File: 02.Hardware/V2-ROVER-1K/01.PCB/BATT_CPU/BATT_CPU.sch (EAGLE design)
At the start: 70 parts, among them K2 FLEX6, Q1 BSS84W-7-F, Q2 BSS84W-7-F, Q3 2N7002PW, Q4 2N7002PW, Q5 2N7002PW, U1 ATSAMD21G18_QFN, U3 TPS78230DDCR, U6 MAX9062EUK+T, U8 SN74LVC1G19DBVR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

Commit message: Update CPU
Colocacion de transistor a la salida del comparador.
"Multiplexado" de la señal del OP_SWITCH
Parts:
- removed R49: 10K, SparkFun-Resistors:RESISTOR0402
- Q5: value 2N7002PW -> BSS84W-7-F; device SparkFun-DiscreteSemi:MOSFET-NCHANNEL2N7002PW -> BSS84W-7-F:BSS84W-7-F
- R18: value (none) -> 100k
- R48: value 100R -> 10k
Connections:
- removed net A0: U1.PA02/EINT2/AIN0/Y0/VOUT
- removed net CPU_EN_DCDC: R18.2, U1.PA16/I2C/I0/SERCOM1+3.0
- removed net IN_UVLO: Q5.G, R48.2, R49.2, U1.PA21/I5/SERCOM3+5.3/I2SFS0
- removed net N$58: R48.1, U6.OUT
- new net CPU_OP_SWITCH: Q5.G, R18.2, U1.PA17/I2C/I1/SERCOM1+3.1
- new net FB_DAC: K2.P$1, U1.PA02/EINT2/AIN0/Y0/VOUT
- new net N$15: U1.PA21/I5/SERCOM3+5.3/I2SFS0
- new net N$16: Q5.D, R18.1, R48.1, U6.OUT
- net EN_DCDC: now also U1.PA16/I2C/I0/SERCOM1+3.0; no longer Q5.D, R18.1
- net GND: no longer Q5.S, R49.1
- net OP_SWITCH: now also Q5.S; no longer U1.PA17/I2C/I1/SERCOM1+3.1
- net VCC: now also R48.2; no longer K2.P$1
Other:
- moved on the sheet: R18, R48

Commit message: revision inicial
corregido rutado del display
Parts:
- R4: value (none) -> 100k
- R5: value (none) -> 47k
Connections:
- net !RES renamed !RES_OLED
- net CPU_OP_SWITCH renamed !CPU_OP_SWITCH
- removed net VDD: C10.1, C22.1, R6.2, U$30.VDD
- net VBAT_LCD: now also Q2.D; no longer Q2.S
- net VBUS: now also Q2.S; no longer Q2.D
- net VCC_2: now also C10.1, C22.1, R6.2, U$30.VDD
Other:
- moved on the sheet: C10, C22, C24, Q2, R6, VBUS, VBUS1, VBUS2, VBUS3, VBUS4

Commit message: Errors Fix
Polaridad PNP.
Señal Rx cambio por TX.
VDD cambio por VCC_2 Display.
ERC y DRC Check
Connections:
- removed net N$11: U1.PA25/I13/SERCOM3+5.3/D+
- removed net N$12: U1.PA28/I8
- removed net N$13: U1.PB03/I3/AIN11/SERCOM5.1
- removed net N$14: U1.PA24/I12/SERCOM3+5.2/D-
- removed net N$15: U1.PA21/I5/SERCOM3+5.3/I2SFS0
- removed net N$8: U1.PA27/I15
- removed net N$9: U1.PA13/I13/I2C/SERCOM2+4.1
- removed net TST_MODE: U1.PA07/I7/AIN7/SERCOM0.3/I2SD0
- removed net VSS: U$30.VSS
- net !RESET: now also VBUS1.TP
- net GND: now also U$30.VSS, VBUS4.TP
- net N$16: now also Q5.S; no longer Q5.D
- net OP_SWITCH: now also Q5.D; no longer Q5.S
- net RXI: no longer K2.P$7
- net SWCLK: now also VBUS2.TP
- net SWDIO: now also VBUS3.TP
- net S_POWER: now also U1.PA21/I5/SERCOM3+5.3/I2SFS0
- net TXO: now also K2.P$7
- net VCC: now also Q1.S, VBUS.TP; no longer Q1.D
- net VCC_2: now also Q1.D; no longer Q1.S
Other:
- note removed: "N/C"
- note removed: "TXLED"
- note removed: "USBHOSTEN"
- moved on the sheet: Q1

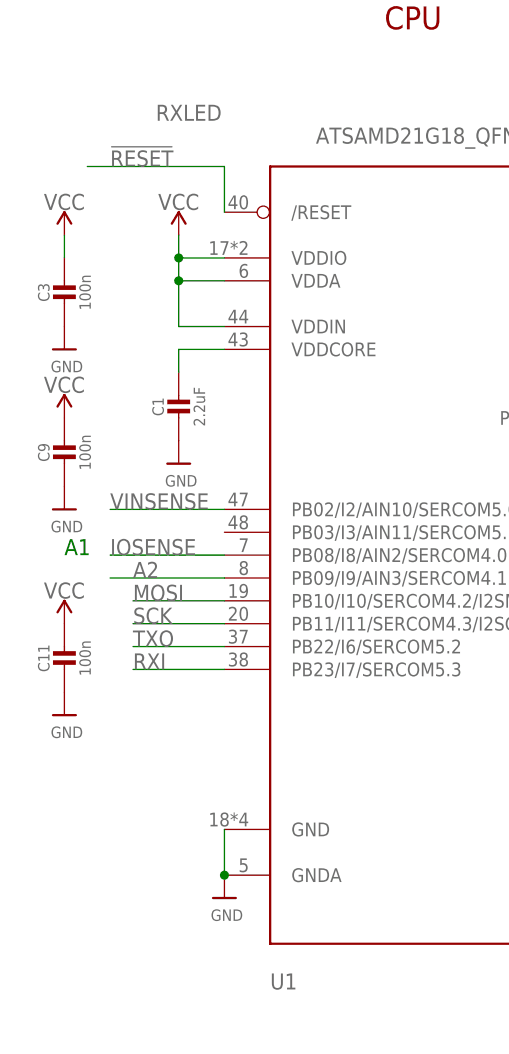
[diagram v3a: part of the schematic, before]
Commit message: Fix errors
DCDC
Recolocacion de los canales RESET y SWCLK
Colocacion resistencia en serie en la linea de RESET.
Recolocacion por espaciado de tornilla.
CPU
Condensador desacoplo linea RESET.
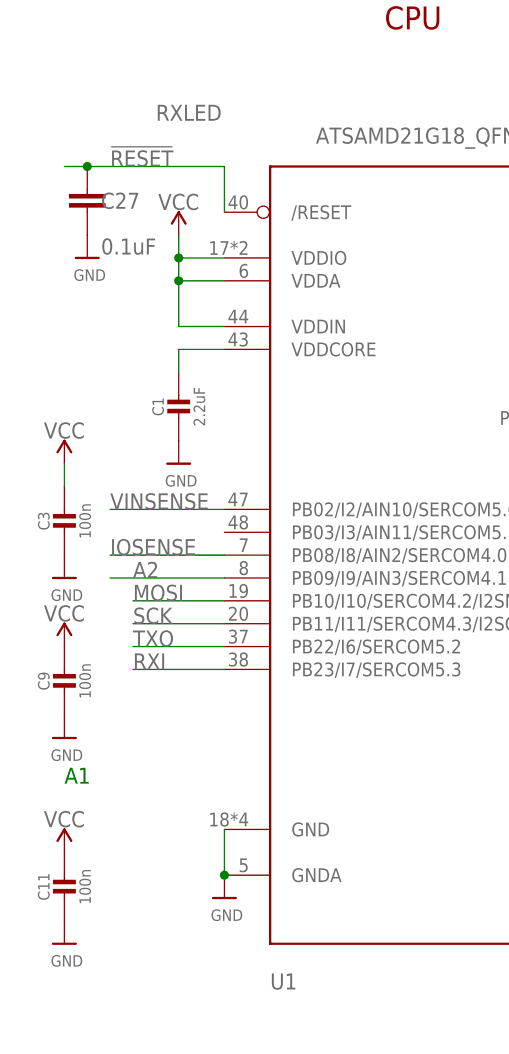
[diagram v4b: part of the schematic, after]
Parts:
- added C27: 0.1uF, SparkFun-Capacitors:0.1UF-0603-25V-5%
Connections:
- net !RESET: now also C27.1
- net GND: now also C27.2
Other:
- moved on the sheet: C11, C3, C9
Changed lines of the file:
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@@
 <part name="R18" library="SparkFun-Resistors" library_urn="urn:adsk.eagle:library:532" deviceset="RESISTOR" device="0402" package3d_urn="urn:adsk.eagle:package:39657/1" value="100k"/>
 <part name="U$31" library="microbuilder" deviceset="GND" device=""/>
+<part name="C27" library="SparkFun-Capacitors" library_urn="urn:adsk.eagle:library:510" deviceset="0.1UF" device="-0603-25V-5%" package3d_urn="urn:adsk.eagle:package:37414/1" value="0.1uF"/>
+<part name="U$32" library="microbuilder" deviceset="GND" device=""/>
 </parts>
 <sheets>
@@
 <text x="106.68" y="45.72" size="1.778" layer="91">D10</text>
 <text x="106.68" y="55.88" size="1.778" layer="91">D2</text>
-<text x="10.16" y="55.88" size="1.778" layer="91">A1</text>
+<text x="10.16" y="30.48" size="1.778" layer="91">A1</text>
 <wire x1="134.62" y1="167.64" x2="261.62" y2="167.64" width="0.1524" layer="94" style="shortdash"/>
 <text x="276.86" y="246.38" size="2.54" layer="94">CHARGING DETECTOR
@@
 <attribute name="VALUE" x="54.356" y="195.58" size="1.27" layer="96"/>
 </instance>
-<instance part="C3" gate="G$1" x="10.16" y="83.82" smashed="yes">
-<attribute name="NAME" x="7.87" y="85.07" size="1.27" layer="95" font="vector" rot="R90" align="center"/>
-<attribute name="VALUE" x="12.46" y="85.07" size="1.27" layer="96" font="vector" rot="R90" align="center"/>
-</instance>
-<instance part="U$7" gate="G$1" x="10.16" y="78.74" smashed="yes">
-<attribute name="VALUE" x="8.636" y="76.2" size="1.27" layer="96"/>
-</instance>
-<instance part="C9" gate="G$1" x="10.16" y="66.04" smashed="yes">
-<attribute name="NAME" x="7.87" y="67.29" size="1.27" layer="95" font="vector" rot="R90" align="center"/>
-<attribute name="VALUE" x="12.46" y="67.29" size="1.27" layer="96" font="vector" rot="R90" align="center"/>
-</instance>
-<instance part="U$14" gate="G$1" x="10.16" y="60.96" smashed="yes">
-<attribute name="VALUE" x="8.636" y="58.42" size="1.27" layer="96"/>
+<instance part="C3" gate="G$1" x="10.16" y="58.42" smashed="yes">
+<attribute name="NAME" x="7.87" y="59.67" size="1.27" layer="95" font="vector" rot="R90" align="center"/>
+<attribute name="VALUE" x="12.46" y="59.67" size="1.27" layer="96" font="vector" rot="R90" align="center"/>
+</instance>
+<instance part="U$7" gate="G$1" x="10.16" y="53.34" smashed="yes">
+<attribute name="VALUE" x="8.636" y="50.8" size="1.27" layer="96"/>
+</instance>
+<instance part="C9" gate="G$1" x="10.16" y="40.64" smashed="yes">
+<attribute name="NAME" x="7.87" y="41.89" size="1.27" layer="95" font="vector" rot="R90" align="center"/>
+<attribute name="VALUE" x="12.46" y="41.89" size="1.27" layer="96" font="vector" rot="R90" align="center"/>
+</instance>
+<instance part="U$14" gate="G$1" x="10.16" y="35.56" smashed="yes">
+<attribute name="VALUE" x="8.636" y="33.02" size="1.27" layer="96"/>
 </instance>
 <instance part="SUPPLY1" gate="G$1" x="73.66" y="223.52" smashed="yes">
 <attribute name="VALUE" x="73.66" y="226.314" size="1.778" layer="96" align="bottom-center"/>
 </instance>
-<instance part="SUPPLY3" gate="G$1" x="10.16" y="91.44" smashed="yes">
-<attribute name="VALUE" x="10.16" y="94.234" size="1.778" layer="96" align="bottom-center"/>
-</instance>
-<instance part="SUPPLY4" gate="G$1" x="10.16" y="71.12" smashed="yes">
-<attribute name="VALUE" x="10.16" y="73.914" size="1.778" layer="96" align="bottom-center"/>
+<instance part="SUPPLY3" gate="G$1" x="10.16" y="66.04" smashed="yes">
+<attribute name="VALUE" x="10.16" y="68.834" size="1.778" layer="96" align="bottom-center"/>
+</instance>
+<instance part="SUPPLY4" gate="G$1" x="10.16" y="45.72" smashed="yes">
+<attribute name="VALUE" x="10.16" y="48.514" size="1.778" layer="96" align="bottom-center"/>
 </instance>
 <instance part="SUPPLY5" gate="G$1" x="22.86" y="91.44" smashed="yes">
@@
 <attribute name="VALUE" x="75.96" y="206.99" size="1.27" layer="96" font="vector" rot="R90" align="center"/>
 </instance>
-<instance part="C11" gate="G$1" x="10.16" y="43.18" smashed="yes">
-<attribute name="NAME" x="7.87" y="44.43" size="1.27" layer="95" font="vector" rot="R90" align="center"/>
-<attribute name="VALUE" x="12.46" y="44.43" size="1.27" layer="96" font="vector" rot="R90" align="center"/>
-</instance>
-<instance part="U$16" gate="G$1" x="10.16" y="38.1" smashed="yes">
-<attribute name="VALUE" x="8.636" y="35.56" size="1.27" layer="96"/>
-</instance>
-<instance part="SUPPLY10" gate="G$1" x="10.16" y="48.26" smashed="yes">
-<attribute name="VALUE" x="10.16" y="51.054" size="1.778" layer="96" align="bottom-center"/>
+<instance part="C11" gate="G$1" x="10.16" y="17.78" smashed="yes">
+<attribute name="NAME" x="7.87" y="19.03" size="1.27" layer="95" font="vector" rot="R90" align="center"/>
+<attribute name="VALUE" x="12.46" y="19.03" size="1.27" layer="96" font="vector" rot="R90" align="center"/>
+</instance>
+<instance part="U$16" gate="G$1" x="10.16" y="12.7" smashed="yes">
+<attribute name="VALUE" x="8.636" y="10.16" size="1.27" layer="96"/>
+</instance>
+<instance part="SUPPLY10" gate="G$1" x="10.16" y="22.86" smashed="yes">
+<attribute name="VALUE" x="10.16" y="25.654" size="1.778" layer="96" align="bottom-center"/>
 </instance>
 <instance part="U6" gate="A" x="299.72" y="220.98" smashed="yes">
@@
 <instance part="U$31" gate="G$1" x="147.32" y="7.62" smashed="yes">
 <attribute name="VALUE" x="145.796" y="5.08" size="1.27" layer="96"/>
+</instance>
+<instance part="C27" gate="G$1" x="12.7" y="93.98" smashed="yes">
+<attribute name="NAME" x="14.224" y="94.361" size="1.778" layer="95"/>
+<attribute name="VALUE" x="14.224" y="89.281" size="1.778" layer="96"/>
+</instance>
+<instance part="U$32" gate="G$1" x="12.7" y="88.9" smashed="yes">
+<attribute name="VALUE" x="11.176" y="86.36" size="1.27" layer="96"/>
 </instance>
 </instances>
@@
 <label x="251.46" y="60.96" size="1.778" layer="95"/>
 </segment>
+<segment>
+<pinref part="U$32" gate="G$1" pin="GND"/>
+<pinref part="C27" gate="G$1" pin="2"/>
+</segment>
 </net>
 <net name="MOSI" class="0">
@@
 <label x="15.24" y="99.06" size="1.778" layer="95"/>
 <wire x1="27.94" y1="99.06" x2="12.7" y2="99.06" width="0.1524" layer="91"/>
+<pinref part="C27" gate="G$1" pin="1"/>
+<wire x1="12.7" y1="99.06" x2="10.16" y2="99.06" width="0.1524" layer="91"/>
+<junction x="12.7" y="99.06"/>
 </segment>
 <segment>
@@
 <pinref part="C3" gate="G$1" pin="1"/>
 <pinref part="SUPPLY3" gate="G$1" pin="VCC"/>
-<wire x1="10.16" y1="91.44" x2="10.16" y2="88.9" width="0.1524" layer="91"/>
-</segment>
-<segment>
+<wire x1="10.16" y1="66.04" x2="10.16" y2="63.5" width="0.1524" layer="91"/>
+</segment>
+<segment>

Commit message: Silk and BOM Review
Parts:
- C1, C14: device microbuilder:CAP_CERAMIC0603_NO -> SparkFun-Capacitors:2.2UF-0603-10V-20%
- C10, C24, C25, C26, C5: value 0.1uF -> 100nF
- C11, C15, C18, C19, C3, C7, C9: value 100n -> 100nF; device microbuilder:CAP_CERAMIC0603_NO -> SparkFun-Capacitors:0.1UF-0402-16V-10%
- C13, C16, C17: value 100n -> 100nF; device rcl:C-EUC0805 -> SparkFun-Capacitors:0.1UF-0402-16V-10%
- C27: value 0.1uF -> 100nF; device SparkFun-Capacitors:0.1UF-0603-25V-5% -> SparkFun-Capacitors:0.1UF-0402-16V-10%
- C6, C8: device microbuilder:CAP_CERAMIC0805-NOOUTLINE -> SparkFun-Capacitors:2.2UF-0603-10V-20%
- R1, R2, R6: value 4K7 -> 4k7
- R16: value (none) -> 100k
- R3: value 560K -> 560k
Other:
- moved on the sheet: C13, C16, C17

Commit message: Revision general
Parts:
- C10, C11, C13, C15, C16, C17, C19, C24, C25, C27, C3, C5, C7, C9: value 100nF -> 100n
- K2: value FLEX6 -> FLEX12
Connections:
- net GND: now also S1.NO_1, S2.NO_1, S3.NO_1
- net N$1: now also S3.COM_1
- net N$3: now also S2.COM_1
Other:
- note added: "5v --> 3v Vo = 3V @Vi=5V vo/vi = 0.6"
- note added: "BATT_CPU ROVER1K NOV'22-v1"
- note removed: "RXLED"
- note removed: "vo/vi = 0.6 5v --> 3v"
- moved on the sheet: C3

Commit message: Revision antes de enviar a SETI
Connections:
- new net VCC_OLED: C21.1, C5.1, U$30.VCC
- net VCC: no longer C21.1, C5.1, U$30.VCC
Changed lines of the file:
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@@
 <text x="106.68" y="45.72" size="1.778" layer="91">D10</text>
 <text x="106.68" y="55.88" size="1.778" layer="91">D2</text>
-<text x="17.78" y="33.02" size="1.778" layer="91">A1</text>
+<text x="20.32" y="33.02" size="1.778" layer="91">A1</text>
 <wire x1="134.62" y1="167.64" x2="261.62" y2="167.64" width="0.1524" layer="94" style="shortdash"/>
 <text x="276.86" y="246.38" size="2.54" layer="94">CHARGING DETECTOR
@@
 </instance>
 <instance part="C14" gate="G$1" x="129.54" y="73.66" smashed="yes">
-<attribute name="NAME" x="127.25" y="74.91" size="1.27" layer="95" font="vector" rot="R90" align="center"/>
-<attribute name="VALUE" x="131.84" y="74.91" size="1.27" layer="96" font="vector" rot="R90" align="center"/>
+<attribute name="NAME" x="125.75" y="78.99" size="1.27" layer="95" font="vector" rot="R180" align="center"/>
+<attribute name="VALUE" x="125.75" y="75.96" size="1.27" layer="96" font="vector" rot="R180" align="center"/>
 </instance>
 <instance part="U$34" gate="G$1" x="297.18" y="17.78" smashed="yes"/>
 <instance part="U$35" gate="G$1" x="292.1" y="17.78" smashed="yes"/>
 <instance part="U1" gate="G$1" x="53.34" y="60.96" smashed="yes">
-<attribute name="NAME" x="33.02" y="7.62" size="1.778" layer="95"/>
+<attribute name="NAME" x="33.02" y="10.16" size="1.778" layer="95"/>
 <attribute name="VALUE" x="38.1" y="101.6" size="1.778" layer="96"/>
 </instance>
@@
 </instance>
 <instance part="C2" gate="G$1" x="109.22" y="109.22" smashed="yes" rot="R180">
-<attribute name="NAME" x="111.51" y="107.97" size="1.27" layer="95" font="vector" rot="R270" align="center"/>
-<attribute name="VALUE" x="106.92" y="107.97" size="1.27" layer="96" font="vector" rot="R270" align="center"/>
+<attribute name="NAME" x="105.39" y="108.97" size="1.27" layer="95" font="vector" align="center"/>
+<attribute name="VALUE" x="105.39" y="106.92" size="1.27" layer="96" font="vector" align="center"/>
 </instance>
 <instance part="C4" gate="G$1" x="119.38" y="109.22" smashed="yes" rot="R180">
-<attribute name="NAME" x="121.67" y="107.97" size="1.27" layer="95" font="vector" rot="R270" align="center"/>
-<attribute name="VALUE" x="117.08" y="107.97" size="1.27" layer="96" font="vector" rot="R270" align="center"/>
+<attribute name="NAME" x="125.71" y="108.97" size="1.27" layer="95" font="vector" align="center"/>
+<attribute name="VALUE" x="125.71" y="106.92" size="1.27" layer="96" font="vector" align="center"/>
 </instance>
 <instance part="U$8" gate="G$1" x="109.22" y="114.3" smashed="yes" rot="R180">
@@
 <wire x1="187.96" y1="60.96" x2="195.58" y2="60.96" width="0.1524" layer="91"/>
 <pinref part="C21" gate="G$1" pin="2"/>
-<wire x1="195.58" y1="60.96" x2="215.9" y2="60.96" width="0.1524" layer="91"/>
+<wire x1="195.58" y1="60.96" x2="205.74" y2="60.96" width="0.1524" layer="91"/>
 <wire x1="215.9" y1="60.96" x2="205.74" y2="60.96" width="0.1524" layer="91"/>
 <wire x1="205.74" y1="60.96" x2="205.74" y2="63.5" width="0.1524" layer="91"/>
@@
 <pinref part="C5" gate="G$1" pin="2"/>
 <wire x1="215.9" y1="63.5" x2="215.9" y2="60.96" width="0.1524" layer="91"/>
-<junction x="215.9" y="60.96"/>
 <pinref part="U$9" gate="G$1" pin="GND"/>
 <pinref part="C20" gate="G$1" pin="2"/>
@@
 </segment>
 <segment>
-<pinref part="U$30" gate="G$1" pin="VCC"/>
-<wire x1="269.24" y1="43.18" x2="248.92" y2="43.18" width="0.1524" layer="91"/>
-<label x="251.46" y="43.18" size="1.778" layer="95"/>
-</segment>
-<segment>
-<wire x1="205.74" y1="76.2" x2="215.9" y2="76.2" width="0.1524" layer="91"/>
-<label x="220.98" y="76.2" size="1.778" layer="95"/>
-<pinref part="C21" gate="G$1" pin="1"/>
-<wire x1="205.74" y1="76.2" x2="205.74" y2="71.12" width="0.1524" layer="91"/>
-<pinref part="C5" gate="G$1" pin="1"/>
-<wire x1="215.9" y1="71.12" x2="215.9" y2="76.2" width="0.1524" layer="91"/>
-<wire x1="215.9" y1="76.2" x2="231.14" y2="76.2" width="0.1524" layer="91"/>
-<junction x="215.9" y="76.2"/>
-</segment>
-<segment>
 <pinref part="R48" gate="G$1" pin="2"/>
 <pinref part="SUPPLY11" gate="G$1" pin="VCC"/>
@@
 </segment>
 </net>
+<net name="VCC_OLED" class="0">
+<segment>
+<wire x1="205.74" y1="76.2" x2="215.9" y2="76.2" width="0.1524" layer="91"/>
+<label x="220.98" y="76.2" size="1.778" layer="95"/>
+<pinref part="C21" gate="G$1" pin="1"/>
+<wire x1="205.74" y1="76.2" x2="205.74" y2="71.12" width="0.1524" layer="91"/>
+<pinref part="C5" gate="G$1" pin="1"/>
+<wire x1="215.9" y1="71.12" x2="215.9" y2="76.2" width="0.1524" layer="91"/>
+<wire x1="215.9" y1="76.2" x2="231.14" y2="76.2" width="0.1524" layer="91"/>
+<junction x="215.9" y="76.2"/>
+</segment>
+<segment>
+<pinref part="U$30" gate="G$1" pin="VCC"/>
+<wire x1="269.24" y1="43.18" x2="248.92" y2="43.18" width="0.1524" layer="91"/>
+<label x="251.46" y="43.18" size="1.778" layer="95"/>
+</segment>
+</net>

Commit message: Actualizacion CPU y PROG_BATT
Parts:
- added VBUS5, VBUS6: TESTPAD_TPSQB1,27, BeagleBone_Blue_R3:TESTPAD_TPSQB1,27
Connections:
- net TXO: now also VBUS6.TP
- net VBUS: now also VBUS5.TP
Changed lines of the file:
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@@
 <drawing>
 <settings>
-<setting alwaysvectorfont="no"/>
+<setting alwaysvectorfont="yes"/>
 <setting keepoldvectorfont="yes"/>
 <setting verticaltext="up"/>
@@
 <part name="C27" library="SparkFun-Capacitors" library_urn="urn:adsk.eagle:library:510" deviceset="0.1UF" device="-0402-16V-10%" package3d_urn="urn:adsk.eagle:package:37413/1" value="100n"/>
 <part name="U$32" library="microbuilder" deviceset="GND" device=""/>
+<part name="VBUS5" library="BeagleBone_Blue_R3" deviceset="TESTPAD_TPSQ" device="B1,27"/>
+<part name="VBUS6" library="BeagleBone_Blue_R3" deviceset="TESTPAD_TPSQ" device="B1,27"/>
 </parts>
 <sheets>
@@
 <attribute name="VALUE" x="11.176" y="86.36" size="1.27" layer="96"/>
 </instance>
+<instance part="VBUS5" gate="G$1" x="322.06" y="103.08" smashed="yes" rot="R270">
+<attribute name="TP_SIGNAL_NAME" x="320.79" y="100.54" size="1.778" layer="97" rot="R270"/>
+</instance>
+<instance part="VBUS6" gate="G$1" x="322.06" y="98" smashed="yes" rot="R270">
+<attribute name="TP_SIGNAL_NAME" x="320.79" y="95.46" size="1.778" layer="97" rot="R270"/>
+</instance>
 </instances>
 <busses>
@@
 <junction x="203.2" y="40.64"/>
 <label x="185.42" y="40.64" size="1.778" layer="95" rot="R180" xref="yes"/>
+</segment>
+<segment>
+<pinref part="VBUS5" gate="G$1" pin="TP"/>
+<wire x1="324.6" y1="103.08" x2="340.36" y2="103.08" width="0.1524" layer="91"/>
+<wire x1="340.36" y1="103.08" x2="340.36" y2="104.14" width="0.1524" layer="91"/>
+<label x="330.2" y="104.14" size="1.778" layer="95"/>
 </segment>
 </net>
@@
 <label x="317.5" y="134.62" size="1.778" layer="95" rot="MR0" align="bottom-right"/>
 </segment>
-</net>
+<segment>
+<pinref part="VBUS6" gate="G$1" pin="TP"/>
+<wire x1="324.6" y1="98" x2="340.36" y2="98" width="0.1524" layer="91"/>
+<wire x1="340.36" y1="98" x2="340.36" y2="99.06" width="0.1524" layer="91"/>
+<label x="330.2" y="99.06" size="1.778" layer="95"/>
+</segment>
+</net>
